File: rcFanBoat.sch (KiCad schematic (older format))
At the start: 1 part

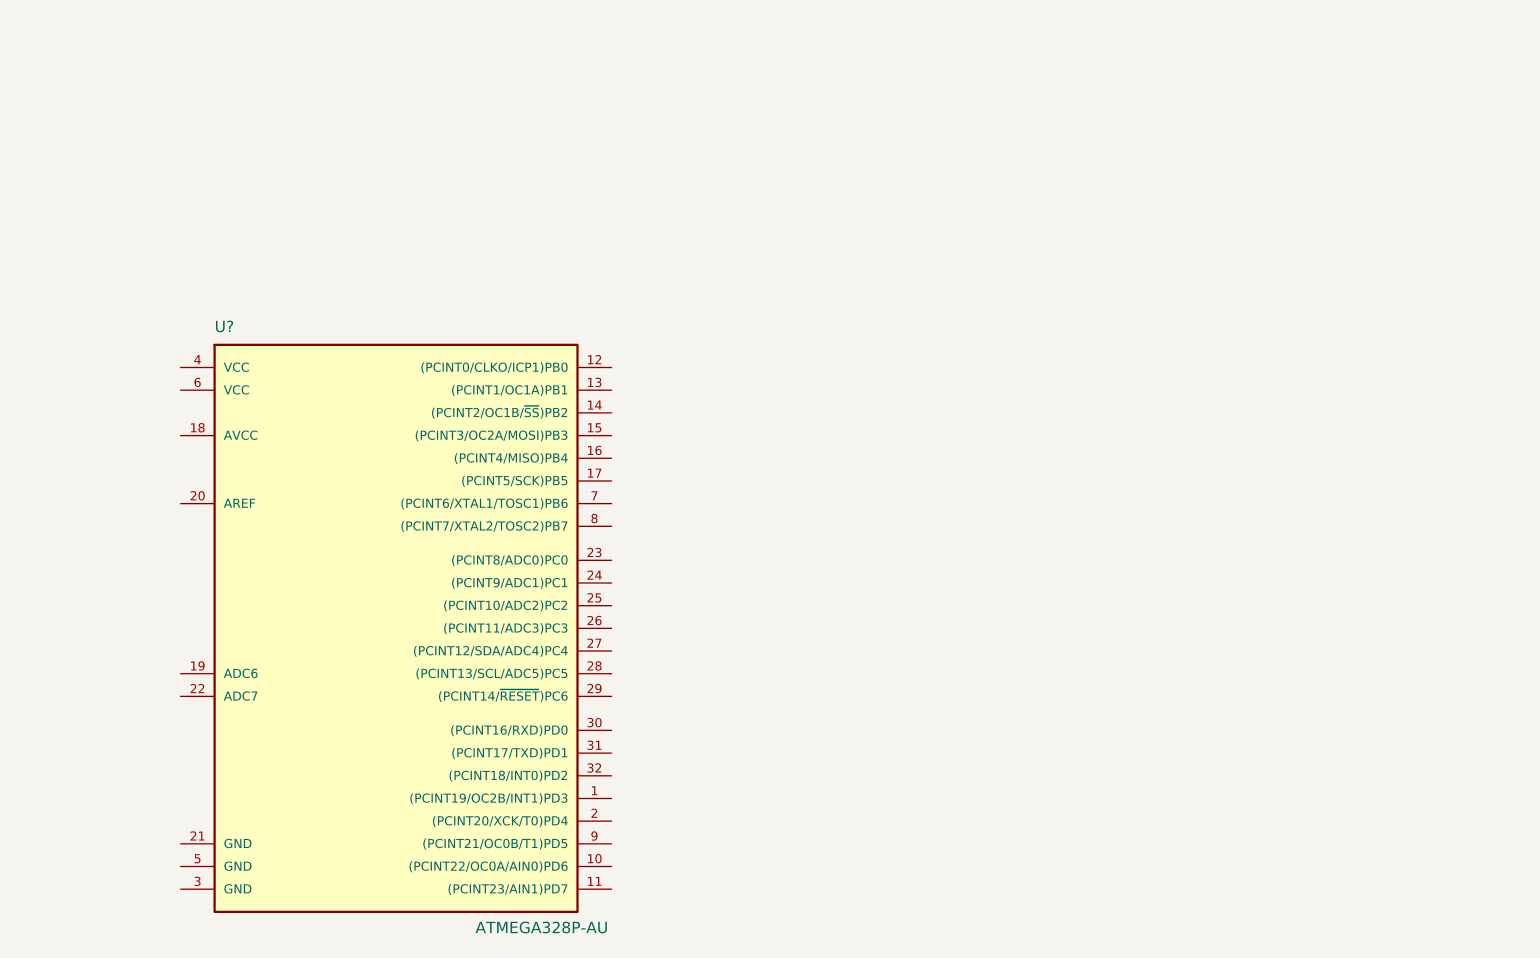
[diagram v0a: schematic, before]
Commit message: add schematic
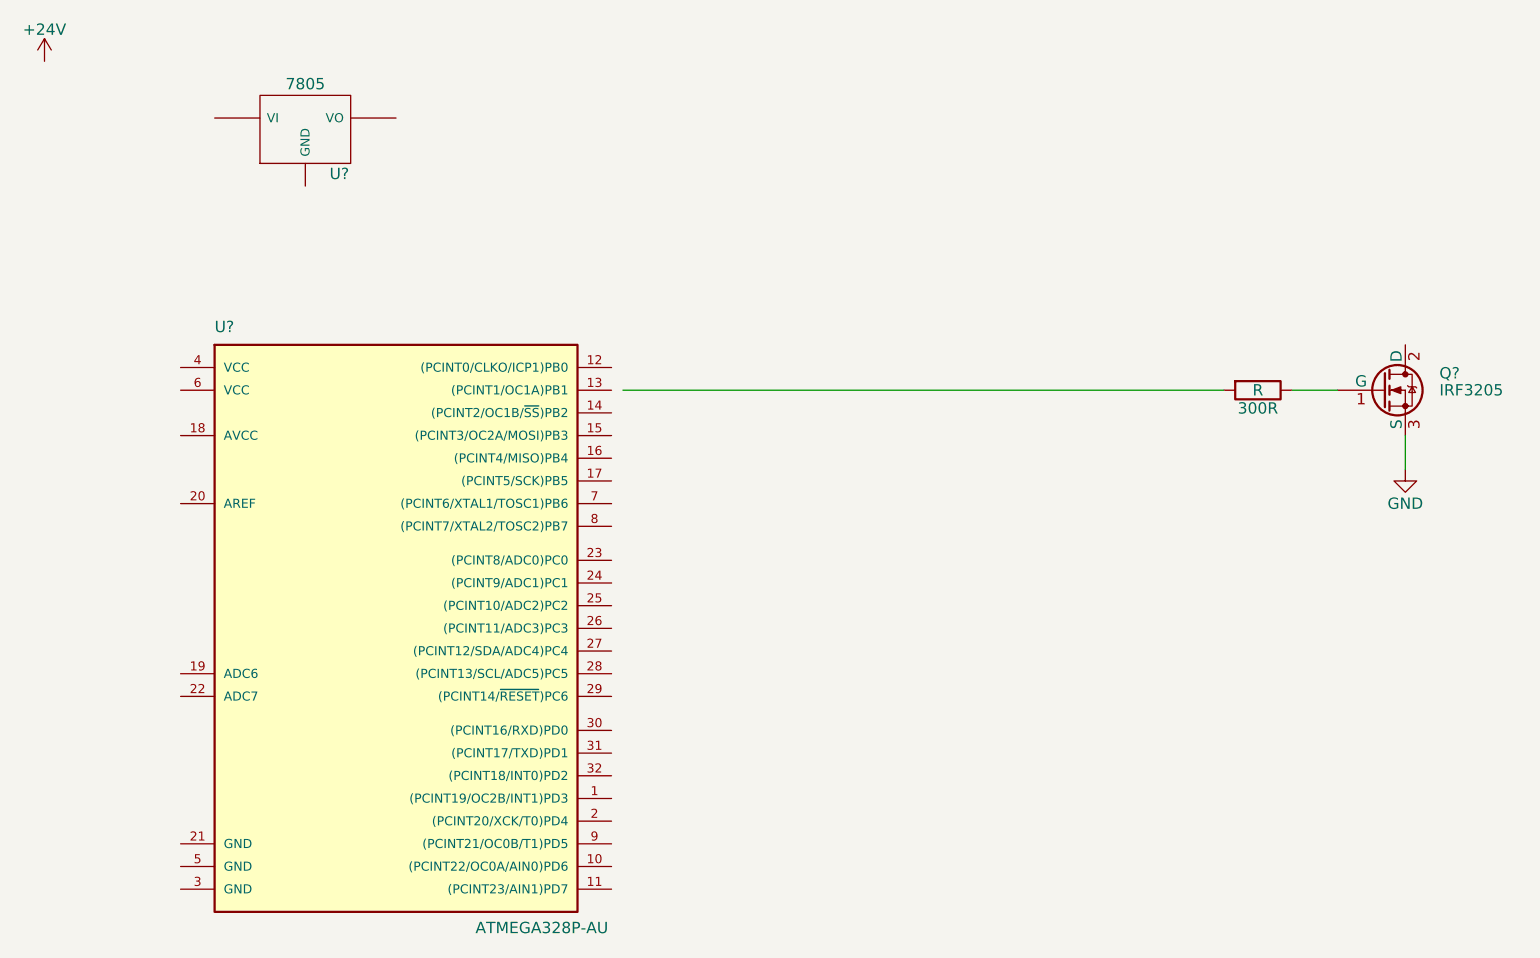
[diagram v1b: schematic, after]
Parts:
- added 300R: R, symbol R
- added Q?: IRF3205, TO_SOT_Packages_THT:TO-220_Vertical, symbol IRF3205
- added U?: 7805, symbol 7805
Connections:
- net labels added: +24V, GND
- wire segments 0 -> 3
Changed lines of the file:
@@
 LIBS:contrib
 LIBS:valves
+LIBS:rcFanBoat-cache
 EELAYER 25 0
 EELAYER END
@@
 	1    0    0    -1
 $EndComp
+$Comp
+L IRF3205 Q?
+U 1 1 5FF1AF36
+P 7000 2350
+F 0 "Q?" H 7250 2425 50  0000 L CNN
+F 1 "IRF3205" H 7250 2350 50  0000 L CNN
+F 2 "TO_SOT_Packages_THT:TO-220_Vertical" H 7250 2275 50  0001 L CIN
+F 3 "" H 7000 2350 50  0001 L CNN
+	1    7000 2350
+	1    0    0    -1
+$EndComp
+$Comp
+L +24V #PWR?
+U 1 1 5FF1B172
+P 1100 900
+F 0 "#PWR?" H 1100 750 50  0001 C CNN
+F 1 "+24V" H 1100 1040 50  0000 C CNN
+F 2 "" H 1100 900 50  0001 C CNN
+F 3 "" H 1100 900 50  0001 C CNN
+	1    1100 900
+	1    0    0    -1
+$EndComp
+$Comp
+L 7805 U?
+U 1 1 5FF1B19D
+P 2250 1200
+F 0 "U?" H 2400 1004 50  0000 C CNN
+F 1 "7805" H 2250 1400 50  0000 C CNN
+F 2 "" H 2250 1200 50  0001 C CNN
+F 3 "" H 2250 1200 50  0001 C CNN
+	1    2250 1200
+	1    0    0    -1
+$EndComp
+$Comp
+L R 300R
+U 1 1 5FF1B1F1
+P 6450 2350
+F 0 "300R" V 6530 2350 50  0000 C CNN
+F 1 "R" V 6450 2350 50  0000 C CNN
+F 2 "" V 6380 2350 50  0001 C CNN
+F 3 "" H 6450 2350 50  0001 C CNN
+	1    6450 2350
+	0    1    1    0
+$EndComp
+Wire Wire Line
+	3650 2350 6300 2350
+Wire Wire Line
+	6600 2350 6800 2350
+$Comp
+L GND #PWR?
+U 1 1 5FF1B58D
+P 7100 2700
+F 0 "#PWR?" H 7100 2450 50  0001 C CNN
+F 1 "GND" H 7100 2550 50  0000 C CNN
+F 2 "" H 7100 2700 50  0001 C CNN
+F 3 "" H 7100 2700 50  0001 C CNN
+	1    7100 2700
+	1    0    0    -1
+$EndComp
+Wire Wire Line
+	7100 2550 7100 2700
 $EndSCHEMATC

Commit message: update schematic
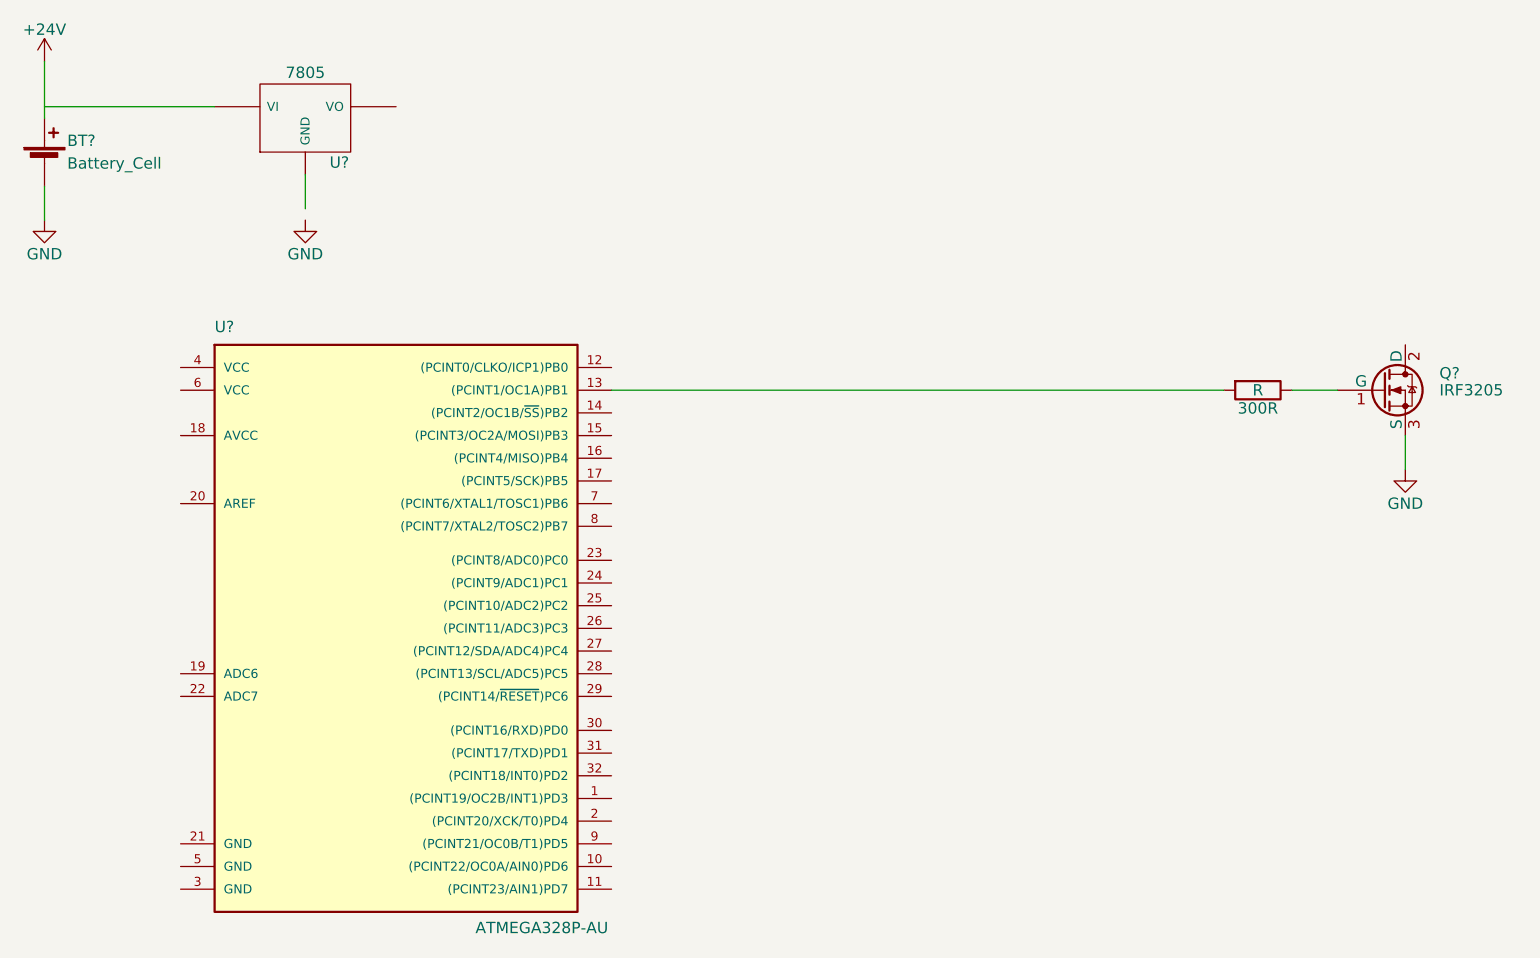
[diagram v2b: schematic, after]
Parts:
- added BT?: Battery_Cell, symbol Battery_Cell
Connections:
- wire segments 3 -> 7
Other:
- moved on the sheet: U?
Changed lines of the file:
@@
 L 7805 U?
 U 1 1 5FF1B19D
-P 2250 1200
-F 0 "U?" H 2400 1004 50  0000 C CNN
-F 1 "7805" H 2250 1400 50  0000 C CNN
-F 2 "" H 2250 1200 50  0001 C CNN
-F 3 "" H 2250 1200 50  0001 C CNN
-	1    2250 1200
+P 2250 1150
+F 0 "U?" H 2400 954 50  0000 C CNN
+F 1 "7805" H 2250 1350 50  0000 C CNN
+F 2 "" H 2250 1150 50  0001 C CNN
+F 3 "" H 2250 1150 50  0001 C CNN
+	1    2250 1150
 	1    0    0    -1
 $EndComp
@@
 $EndComp
 Wire Wire Line
-	3650 2350 6300 2350
+	3600 2350 6300 2350
 Wire Wire Line
 	6600 2350 6800 2350
@@
 Wire Wire Line
 	7100 2550 7100 2700
+$Comp
+L GND #PWR?
+U 1 1 5FF1BB5B
+P 2250 1600
+F 0 "#PWR?" H 2250 1350 50  0001 C CNN
+F 1 "GND" H 2250 1450 50  0000 C CNN
+F 2 "" H 2250 1600 50  0001 C CNN
+F 3 "" H 2250 1600 50  0001 C CNN
+	1    2250 1600
+	1    0    0    -1
+$EndComp
+Wire Wire Line
+	2250 1550 2250 1400
+$Comp
+L Battery_Cell BT?
+U 1 1 5FF1BC83
+P 1100 1350
+F 0 "BT?" H 1200 1450 50  0000 L CNN
+F 1 "Battery_Cell" H 1200 1350 50  0000 L CNN
+F 2 "" V 1100 1410 50  0001 C CNN
+F 3 "" V 1100 1410 50  0001 C CNN
+	1    1100 1350
+	1    0    0    -1
+$EndComp
+$Comp
+L GND #PWR?
+U 1 1 5FF1BCD5
+P 1100 1600
+F 0 "#PWR?" H 1100 1350 50  0001 C CNN
+F 1 "GND" H 1100 1450 50  0000 C CNN
+F 2 "" H 1100 1600 50  0001 C CNN
+F 3 "" H 1100 1600 50  0001 C CNN
+	1    1100 1600
+	1    0    0    -1
+$EndComp
+Wire Wire Line
+	1100 1600 1100 1450
+Wire Wire Line
+	1100 900  1100 1150
+Wire Wire Line
+	1100 1100 1850 1100
 $EndSCHEMATC
